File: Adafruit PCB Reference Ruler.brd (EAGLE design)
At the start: 154.9 x 25.4 mm, 71 parts

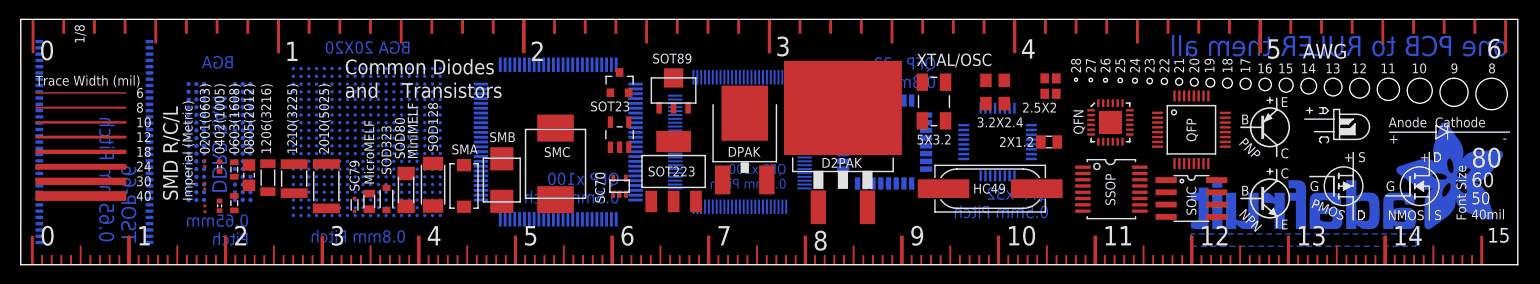
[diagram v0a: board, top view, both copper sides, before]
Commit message: Customizing for distribution in my class: 1. Removed adafruit logo assuming it's copyrighted 2. added text to credit ownership/license 3. added securinghardware.com logo 4. replaced binary with decimal inch fractions 5. moved both inch and cm scales to align with edge of ruler
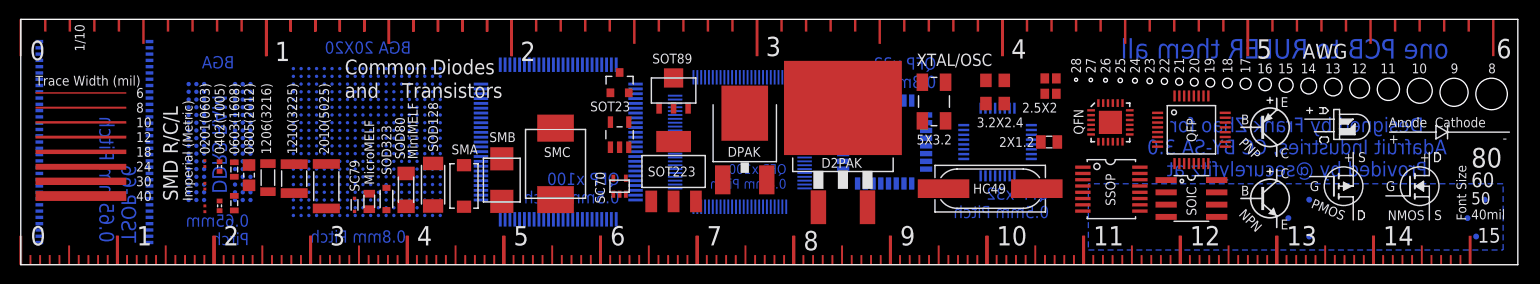
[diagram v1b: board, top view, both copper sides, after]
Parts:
- removed E$22: (no value), Reference Ruler:EDGE-INCHES-EIGTH
- added E$64, E$73: (no value), newinches:INCHES
- E$17, E$18, E$19, E$20, E$21: device Reference Ruler:EDGE-INCHES-EIGTH -> newinches:INCHES
- E$72: device Reference Ruler:ADAFRUIT-LOGO-0.5IN -> securinghardware:SECURINGHARDWAREDOTCOM
- moved E$19 24.1 mm to (76.2, 25.4)
- moved E$18 24.1 mm to (50.8, 25.4)
- moved E$20 24.1 mm to (101.6, 25.4)
- moved E$21 24.1 mm to (127.0, 25.4)
- moved E$17 1.27 mm to (0.00, 25.4)
- moved E$10 1.20 mm to (90.0, 0.00)
- moved E$11 1.20 mm to (100.0, 0.00)
- moved E$12 1.20 mm to (110.0, 0.00)
- moved E$13 1.20 mm to (120.0, 0.00)
- moved E$5 1.20 mm to (40.0, 0.00)
- moved E$6 1.20 mm to (50.0, 0.00)
- moved E$7 1.20 mm to (60.0, 0.00)
- moved E$8 1.20 mm to (70.0, 0.00)
- moved E$9 1.20 mm to (80.0, 0.00)
- moved E$1 1.20 mm to (0.00, 0.00)
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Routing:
- added copper zone on layer 16, net GND
- removed copper zone on layer 16, net S$1
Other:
- board text added: "1/10"
- board text added: "Designed by Frank Zhao for Adafruit Industries, CC BY-SA 3.0 Provided by @securelyfitz at"
- board text removed: "1/8"
